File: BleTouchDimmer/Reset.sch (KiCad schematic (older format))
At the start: 3 parts, among them SW1 SW_PUSH

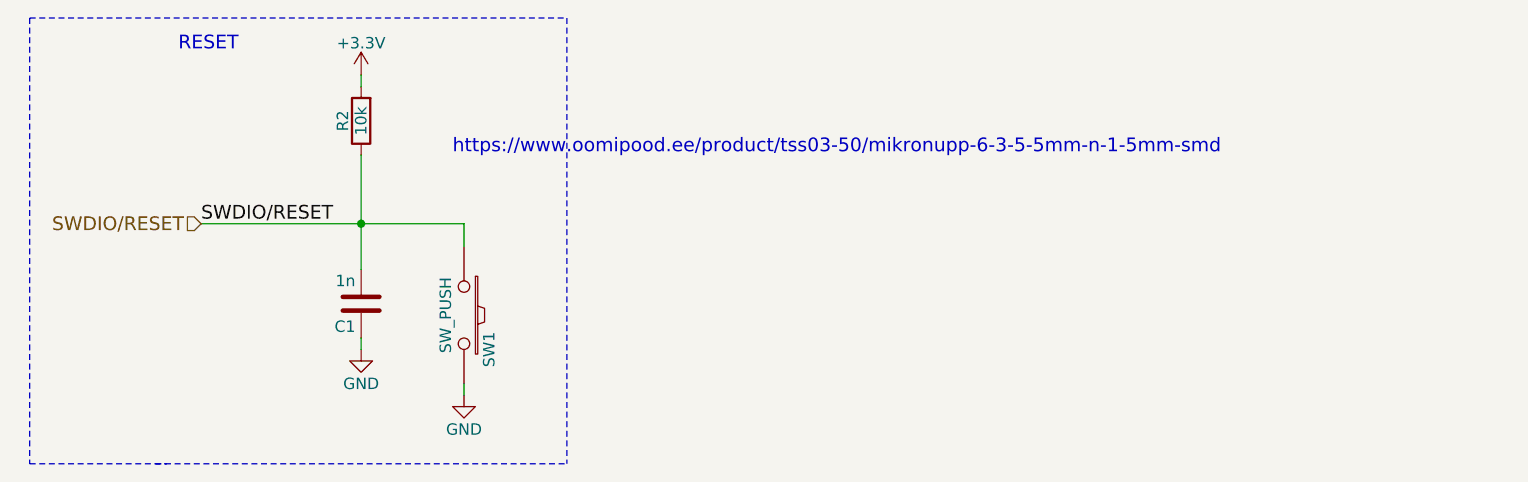
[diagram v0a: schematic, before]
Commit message: Added triacs.
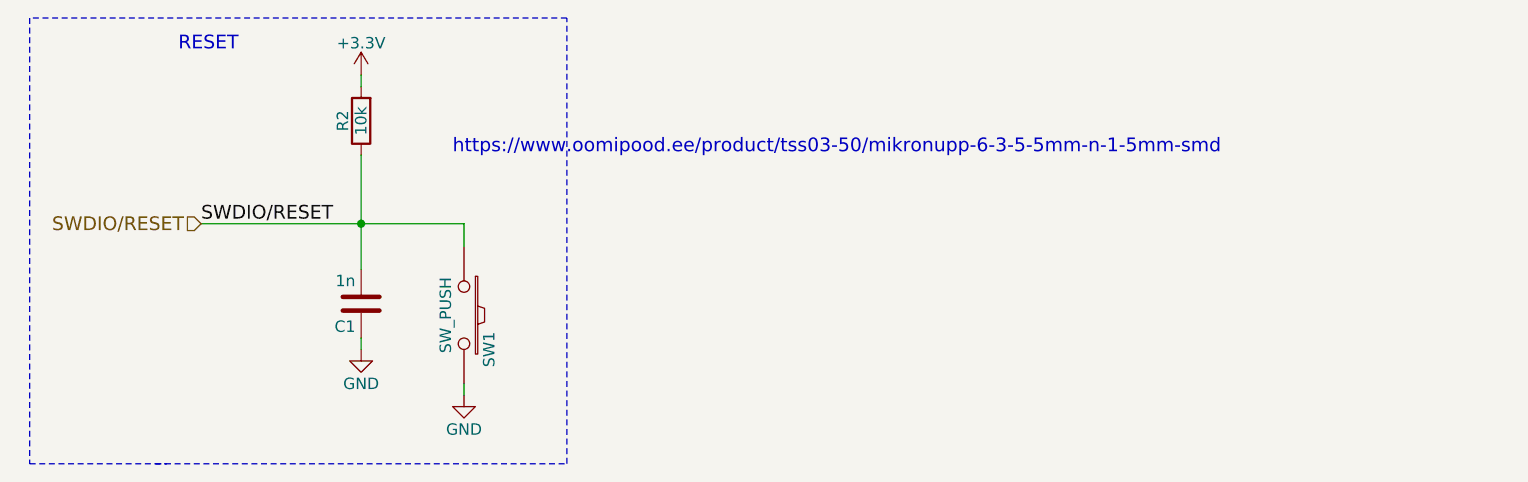
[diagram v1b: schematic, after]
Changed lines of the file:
@@
 $EndComp
 $Comp
-L +3.3V #PWR21
+L +3.3V #PWR023
 U 1 1 582107D1
 P 5700 2700
-F 0 "#PWR21" H 5700 2550 50  0001 C CNN
+F 0 "#PWR023" H 5700 2550 50  0001 C CNN
 F 1 "+3.3V" H 5700 2840 50  0000 C CNN
 F 2 "" H 5700 2700 50  0000 C CNN
@@
 	6150 3350 6150 3450
 $Comp
-L GND #PWR23
+L GND #PWR024
 U 1 1 582107EB
 P 6150 4100
-F 0 "#PWR23" H 6150 3850 50  0001 C CNN
+F 0 "#PWR024" H 6150 3850 50  0001 C CNN
 F 1 "GND" H 6150 3950 50  0000 C CNN
 F 2 "" H 6150 4100 50  0000 C CNN
@@
 	5000 3350 6150 3350
 $Comp
-L GND #PWR22
+L GND #PWR025
 U 1 1 582107F4
 P 5700 3900
-F 0 "#PWR22" H 5700 3650 50  0001 C CNN
+F 0 "#PWR025" H 5700 3650 50  0001 C CNN
 F 1 "GND" H 5700 3750 50  0000 C CNN
 F 2 "" H 5700 3900 50  0000 C CNN
@@
 	4800 4400 6600 4400
 Wire Notes Line
-	6600 2450 6600 4400
+	6600 4400 6600 2450
 Wire Notes Line
-	4250 2450 6600 2450
+	6600 2450 4250 2450
 Text Notes 4900 2600 0    60   ~ 0
 RESET

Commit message: Uncommited changes.
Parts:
- C1: footprint Capacitors_SMD:C_0805 -> Capacitors_SMD:C_0603
- R2: footprint Resistors_SMD:R_0805 -> Resistors_SMD:R_0603
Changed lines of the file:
@@
 EESchema Schematic File Version 2
+LIBS:BleTouchDimmer-rescue
+LIBS:cypress_touch
+LIBS:azoteq_touch
 LIBS:power
 LIBS:device
@@
 LIBS:Symbols_Microcontroller_Philips-NXP_RevA_06Oct2013
 LIBS:nordicsemi
-LIBS:Egert
 LIBS:Oscillators
 LIBS:74xgxx
@@
 LIBS:microchip_pic16mcu
 LIBS:microchip_pic18mcu
-LIBS:microchip_pic32mcu
 LIBS:motor_drivers
 LIBS:motors
@@
 LIBS:SymbolsSimilarEN60617+oldDIN617-RevE8
 LIBS:BleTouchDimmer-cache
-EELAYER 25 0
+EELAYER 26 0
 EELAYER END
 $Descr A4 11693 8268
@@
 F 0 "R2" V 5780 2900 50  0000 C CNN
 F 1 "10k" V 5700 2900 50  0000 C CNN
-F 2 "Resistors_SMD:R_0805" V 5630 2900 50  0001 C CNN
+F 2 "Resistors_SMD:R_0603" V 5630 2900 50  0001 C CNN
 F 3 "" H 5700 2900 50  0000 C CNN
 	1    5700 2900
@@
 F 0 "C1" H 5725 3800 50  0000 L CNN
 F 1 "1n" H 5725 3600 50  0000 L CNN
-F 2 "Capacitors_SMD:C_0805" H 5738 3550 50  0001 C CNN
+F 2 "Capacitors_SMD:C_0603" H 5738 3550 50  0001 C CNN
 F 3 "" H 5700 3700 50  0000 C CNN
 	1    5700 3700
